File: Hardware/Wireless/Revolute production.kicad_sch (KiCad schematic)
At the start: 58 parts, among them J1 -, J2 +, Q1 NMOS-CSD17381F4, Q2 NMOS-CSD17381F4, Q3 PMOS-CSD25483F4, Q4 PMOS-CSD25483F4, Q5 PMOS-CSD25483F4, SW1 SW_Omron_B3FS, U10 BQ24075RGT, U11 MIC5504, U5 BQ27427, U6 nrf52833_qfn40, U8 Conn_01x14_Socket, U9 AS5600, X1 32.768 kHz, X2 32MHZ

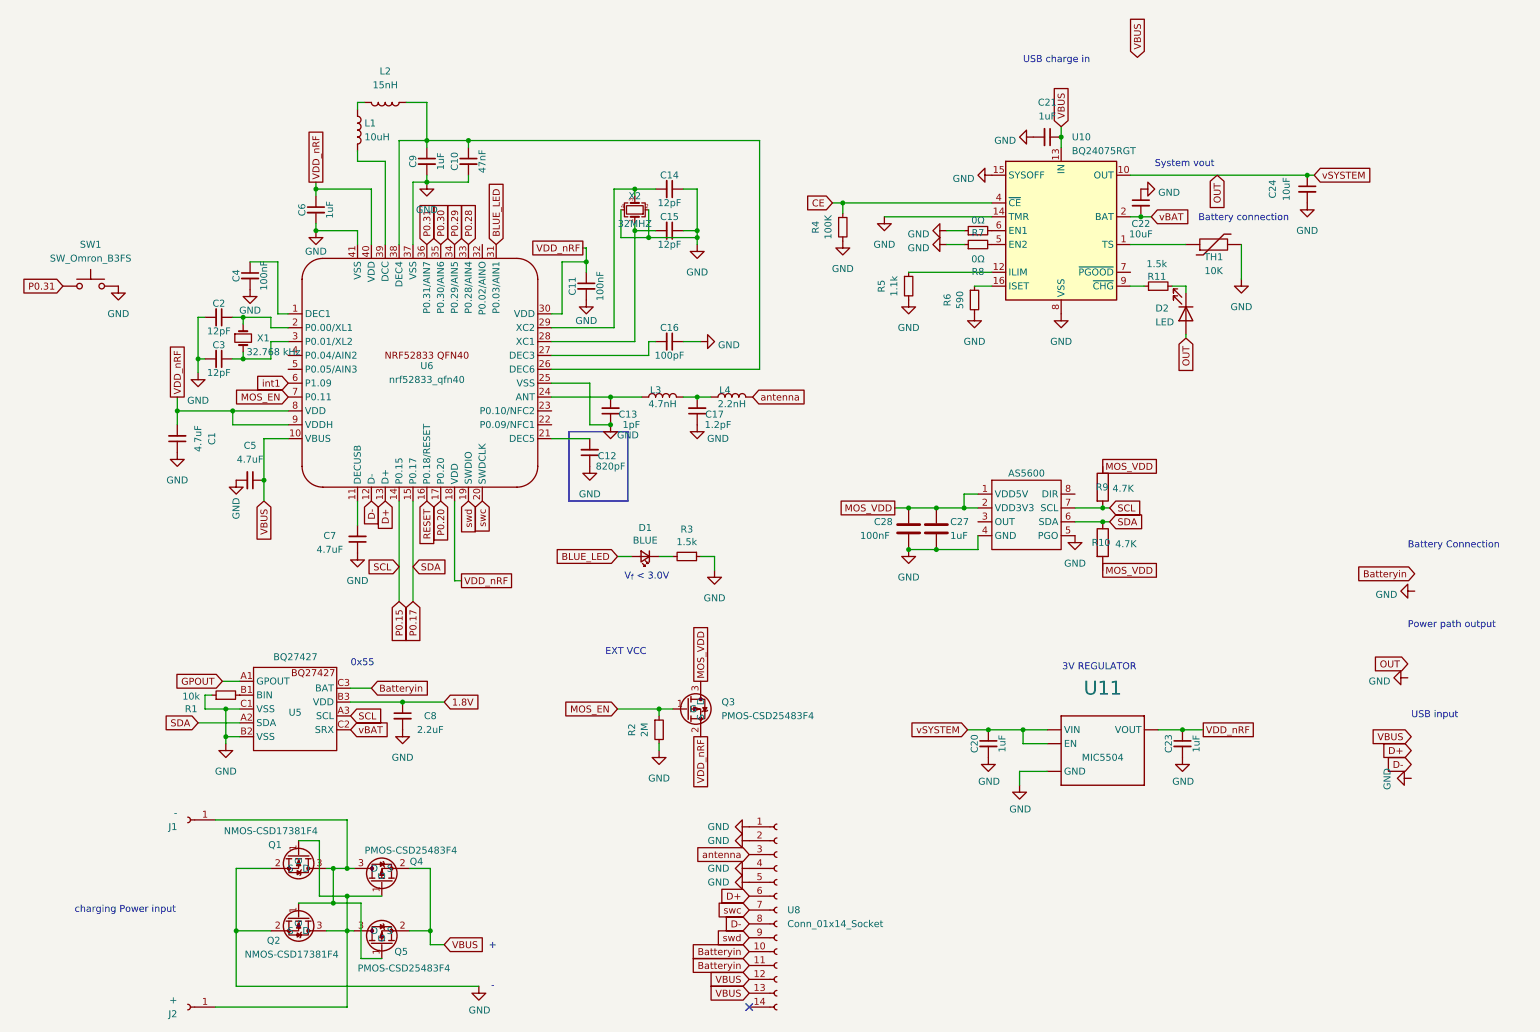
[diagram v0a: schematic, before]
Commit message: added status led
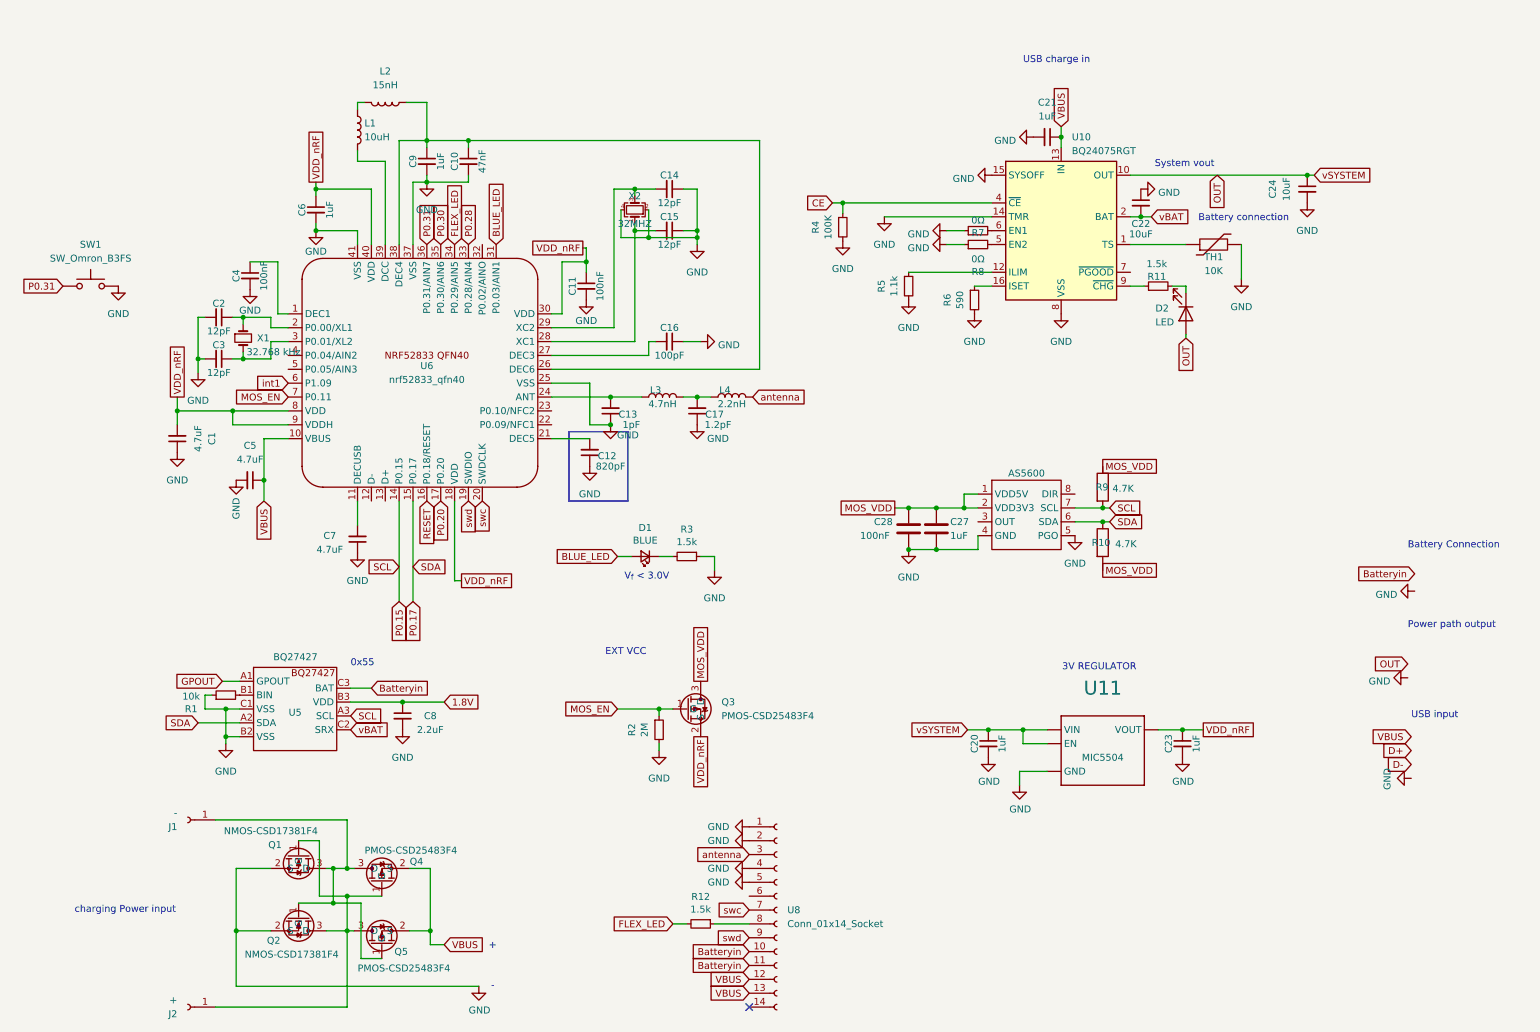
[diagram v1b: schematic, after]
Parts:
- added R12: 1.5k, Library:0402, symbol Device:R_Small
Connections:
- net D+: no longer U6.13 (D+), U8.6 (Pin_6)
- net D-: no longer U6.12 (D-), U8.8 (Pin_8)
- net P0.29 renamed FLEX_LED
- net FLEX_LED: now also R12.2
- new net: R12.1, U8.8 (Pin_8)
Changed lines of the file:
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@@
 	(wire
 		(pts
+			(xy 130.81 175.26) (xy 133.35 175.26)
+		)
+		(stroke
+			(width 0)
+			(type default)
+		)
+	)
+	(wire
+		(pts
 			(xy 214.63 58.42) (xy 217.17 58.42)
 		)
@@
 	(wire
 		(pts
+			(xy 138.43 175.26) (xy 144.78 175.26)
+		)
+		(stroke
+			(width 0)
+			(type default)
+		)
+	)
+	(wire
+		(pts
 			(xy 85.725 38.1) (xy 85.725 39.37)
 		)
@@
 		)
 	)
-	(global_label "D+"
-		(shape input)
-		(at 144.78 170.18 180)
-		(fields_autoplaced yes)
-		(effects
-			(font
-				(size 1.27 1.27)
-			)
-			(justify right)
-		)
-		(property "Intersheetrefs" "${INTERSHEET_REFS}"
-			(at 138.9524 170.18 0)
-			(effects
-				(font
-					(size 1.27 1.27)
-				)
-				(justify right)
-				(hide yes)
-			)
-		)
-	)
 	(global_label "RESET"
 		(shape input)
@@
 		)
 	)
-	(global_label "D-"
-		(shape input)
-		(at 75.565 97.79 270)
-		(fields_autoplaced yes)
-		(effects
-			(font
-				(size 1.27 1.27)
-			)
-			(justify right)
-		)
-		(property "Intersheetrefs" "${INTERSHEET_REFS}"
-			(at 75.565 103.5382 90)
-			(effects
-				(font
-					(size 1.27 1.27)
-				)
-				(justify right)
-				(hide yes)
-			)
-		)
-	)
 	(global_label "Batteryin"
 		(shape input)
@@
 		)
 	)
-	(global_label "D-"
-		(shape input)
-		(at 144.78 175.26 180)
-		(fields_autoplaced yes)
-		(effects
-			(font
-				(size 1.27 1.27)
-			)
-			(justify right)
-		)
-		(property "Intersheetrefs" "${INTERSHEET_REFS}"
-			(at 138.9524 175.26 0)
-			(effects
-				(font
-					(size 1.27 1.27)
-				)
-				(justify right)
-				(hide yes)
-			)
-		)
-	)
 	(global_label "vBAT"
 		(shape input)
@@
 		)
 	)
-	(global_label "D+"
-		(shape input)
-		(at 78.105 97.79 270)
-		(fields_autoplaced yes)
-		(effects
-			(font
-				(size 1.27 1.27)
-			)
-			(justify right)
-		)
-		(property "Intersheetrefs" "${INTERSHEET_REFS}"
-			(at 78.105 103.5382 90)
-			(effects
-				(font
-					(size 1.27 1.27)
-				)
-				(justify right)
-				(hide yes)
-			)
-		)
-	)
 	(global_label "MOS_VDD"
 		(shape passive)
@@
 		)
 	)
-	(global_label "VBUS"
-		(shape input)
-		(at 215.9 16.51 90)
-		(fields_autoplaced yes)
-		(effects
-			(font
-				(size 1.27 1.27)
-			)
-			(justify left)
-		)
-		(property "Intersheetrefs" "${INTERSHEET_REFS}"
-			(at 215.9 8.7056 90)
-			(effects
-				(font
-					(size 1.27 1.27)
-				)
-				(justify left)
-				(hide yes)
-			)
-		)
-	)
 	(global_label "CE"
 		(shape input)
@@
 		)
 	)
-	(global_label "P0.29"
-		(shape input)
-		(at 90.805 50.8 90)
-		(fields_autoplaced yes)
-		(effects
-			(font
-				(size 1.27 1.27)
-			)
-			(justify left)
-		)
-		(property "Intersheetrefs" "${INTERSHEET_REFS}"
-			(at 90.805 42.3909 90)
-			(effects
-				(font
-					(size 1.27 1.27)
-				)
-				(justify left)
-				(hide yes)
-			)
-		)
-	)
 	(global_label "VDD_nRF"
 		(shape passive)
@@
 		)
 	)
+	(global_label "FLEX_LED"
+		(shape input)
+		(at 130.81 175.26 180)
+		(fields_autoplaced yes)
+		(effects
+			(font
+				(size 1.27 1.27)
+			)
+			(justify right)
+		)
+		(property "Intersheetrefs" "${INTERSHEET_REFS}"
+			(at 118.9349 175.26 0)
+			(effects
+				(font
+					(size 1.27 1.27)
+				)
+				(justify right)
+				(hide yes)
+			)
+		)
+	)
+	(global_label "FLEX_LED"
+		(shape input)
+		(at 90.805 50.8 90)
+		(fields_autoplaced yes)
+		(effects
+			(font
+				(size 1.27 1.27)
+			)
+			(justify left)
+		)
+		(property "Intersheetrefs" "${INTERSHEET_REFS}"
+			(at 90.805 38.9249 90)
+			(effects
+				(font
+					(size 1.27 1.27)
+				)
+				(justify left)
+				(hide yes)
+			)
+		)
+	)
 	(global_label "VDD_nRF"
 		(shape passive)
@@
 					(unit 1)
 				)
+			)
+		)
+	)
+	(symbol
+		(lib_id "Device:R_Small")
+		(at 135.89 175.26 270)
+		(unit 1)
+		(exclude_from_sim no)
+		(in_bom yes)
+		(on_board yes)
+		(dnp no)
+		(property "Reference" "R12"
+			(at 135.89 170.2816 90)
+			(effects
+				(font
+					(size 1.27 1.27)
+				)
+			)
+		)
+		(property "Value" "1.5k"
+			(at 135.89 172.593 90)
+			(effects
+				(font
+					(size 1.27 1.27)
+				)
+			)
+		)
+		(property "Footprint" "Library:0402"
+			(at 135.89 175.26 0)
+			(effects
+				(font
+					(size 1.27 1.27)
+				)
+				(hide yes)
+			)
+		)
+		(property "Datasheet" "~"
+			(at 135.89 175.26 0)
+			(effects
+				(font
+					(size 1.27 1.27)
+				)
+				(hide yes)
+			)
+		)
+		(property "Description" "Resistor, small symbol"
+			(at 135.89 175.26 0)
+			(effects
+				(font
+					(size 1.27 1.27)
+				)
+				(hide yes)
+			)
+		)
+		(property "ID" "138"
+			(at 135.89 175.26 90)
+			(effects
+				(font
+					(size 1.27 1.27)
+				)
+				(hide yes)
+			)
+		)
+		(pin "1"
+		)
+		(pin "2"
+		)
+		(instances
+			(project "Revolute production"
+				(path "/4aa15f71-f105-4387-ae73-e687df291edc"
+					(reference "R12")
+					(unit 1)
+				)

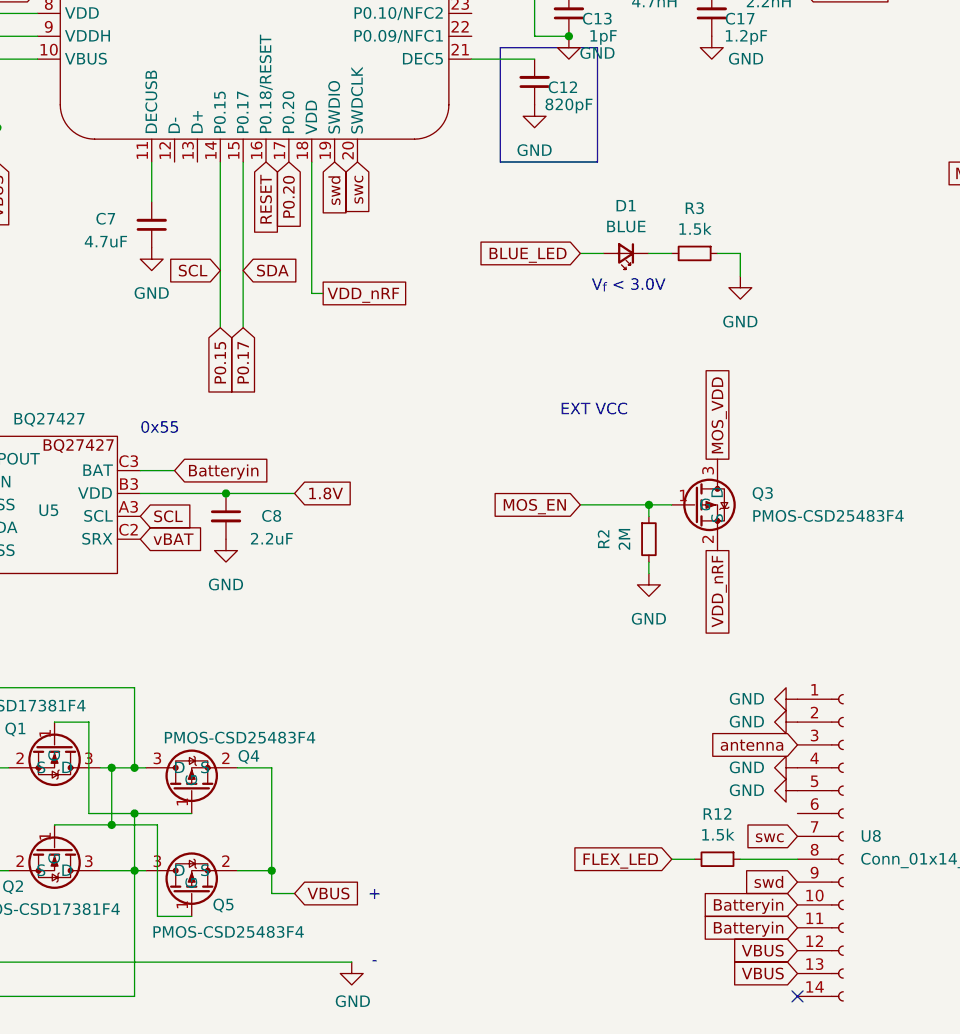
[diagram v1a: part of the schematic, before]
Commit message: revolute production boards
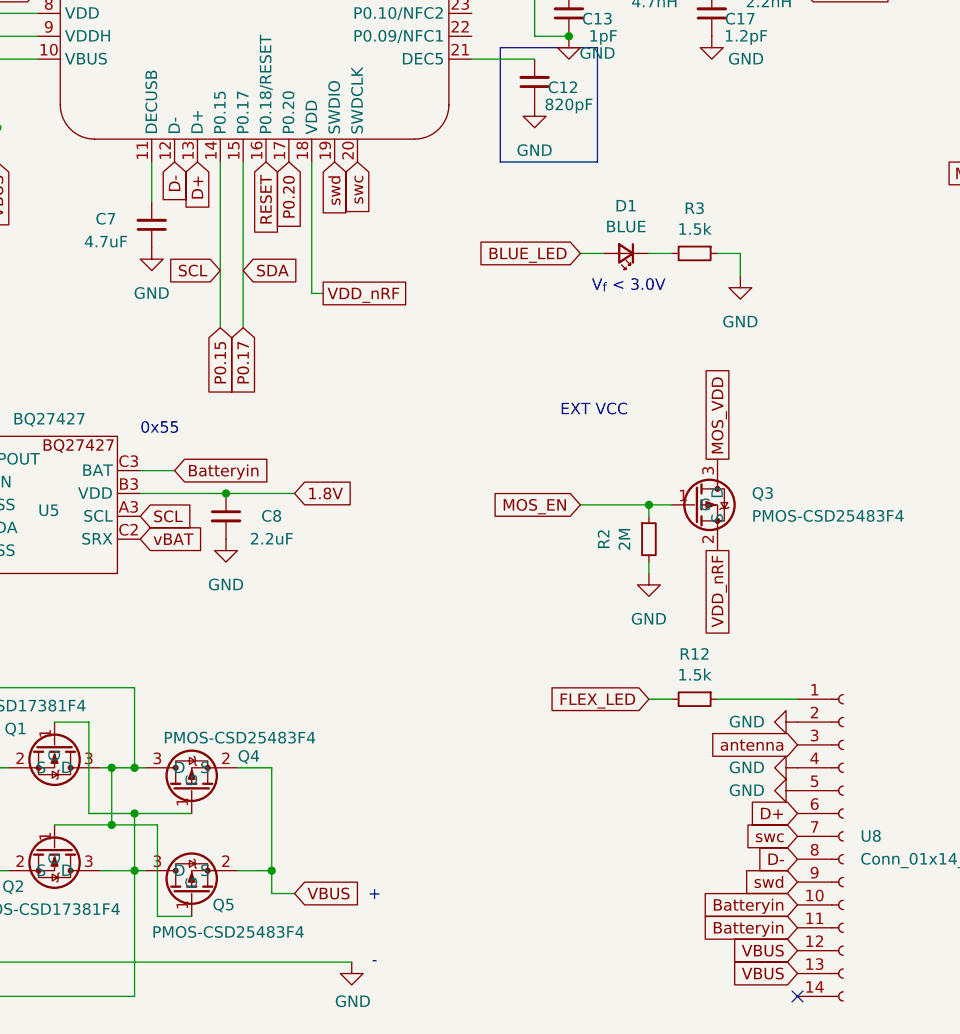
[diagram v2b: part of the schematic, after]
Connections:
- net D+: now also U6.13 (D+), U8.6 (Pin_6)
- net D-: now also U6.12 (D-), U8.8 (Pin_8)
- net GND: no longer U8.1 (Pin_1)
- net at R12.1: now also U8.1 (Pin_1); no longer U8.8 (Pin_8)
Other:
- moved on the sheet: R12
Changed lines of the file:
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@@
 	(wire
 		(pts
-			(xy 130.81 175.26) (xy 133.35 175.26)
+			(xy 128.27 157.48) (xy 130.81 157.48)
 		)
 		(stroke
@@
 	(wire
 		(pts
-			(xy 138.43 175.26) (xy 144.78 175.26)
+			(xy 135.89 157.48) (xy 144.78 157.48)
 		)
 		(stroke
@@
 		)
 	)
+	(global_label "D-"
+		(shape input)
+		(at 144.78 175.26 180)
+		(fields_autoplaced yes)
+		(effects
+			(font
+				(size 1.27 1.27)
+			)
+			(justify right)
+		)
+		(property "Intersheetrefs" "${INTERSHEET_REFS}"
+			(at 138.9524 175.26 0)
+			(effects
+				(font
+					(size 1.27 1.27)
+				)
+				(justify right)
+				(hide yes)
+			)
+		)
+	)
 	(global_label "OUT"
 		(shape input)
@@
 		)
 	)
+	(global_label "D+"
+		(shape input)
+		(at 78.105 97.79 270)
+		(fields_autoplaced yes)
+		(effects
+			(font
+				(size 1.27 1.27)
+			)
+			(justify right)
+		)
+		(property "Intersheetrefs" "${INTERSHEET_REFS}"
+			(at 78.105 103.5382 90)
+			(effects
+				(font
+					(size 1.27 1.27)
+				)
+				(justify right)
+				(hide yes)
+			)
+		)
+	)
+	(global_label "D-"
+		(shape input)
+		(at 75.565 97.79 270)
+		(fields_autoplaced yes)
+		(effects
+			(font
+				(size 1.27 1.27)
+			)
+			(justify right)
+		)
+		(property "Intersheetrefs" "${INTERSHEET_REFS}"
+			(at 75.565 103.5382 90)
+			(effects
+				(font
+					(size 1.27 1.27)
+				)
+				(justify right)
+				(hide yes)
+			)
+		)
+	)
 	(global_label "P0.31"
 		(shape input)
@@
 		)
 	)
+	(global_label "D+"
+		(shape input)
+		(at 144.78 170.18 180)
+		(fields_autoplaced yes)
+		(effects
+			(font
+				(size 1.27 1.27)
+			)
+			(justify right)
+		)
+		(property "Intersheetrefs" "${INTERSHEET_REFS}"
+			(at 138.9524 170.18 0)
+			(effects
+				(font
+					(size 1.27 1.27)
+				)
+				(justify right)
+				(hide yes)
+			)
+		)
+	)
 	(global_label "VBUS"
 		(shape input)
@@
 	(global_label "FLEX_LED"
 		(shape input)
-		(at 130.81 175.26 180)
+		(at 128.27 157.48 180)
 		(fields_autoplaced yes)
 		(effects
@@
 		)
 		(property "Intersheetrefs" "${INTERSHEET_REFS}"
-			(at 118.9349 175.26 0)
+			(at 116.3949 157.48 0)
 			(effects
 				(font
@@
 	(symbol
 		(lib_id "Device:R_Small")
-		(at 135.89 175.26 270)
+		(at 133.35 157.48 270)
 		(unit 1)
 		(exclude_from_sim no)
@@
 		(dnp no)
 		(property "Reference" "R12"
-			(at 135.89 170.2816 90)
+			(at 133.35 152.5016 90)
 			(effects
 				(font
@@
 		)
 		(property "Value" "1.5k"
-			(at 135.89 172.593 90)
+			(at 133.35 154.813 90)
 			(effects
 				(font
@@
 		)
 		(property "Footprint" "Library:0402"
-			(at 135.89 175.26 0)
+			(at 133.35 157.48 0)
 			(effects
 				(font
@@
 		)
 		(property "Datasheet" "~"
-			(at 135.89 175.26 0)
+			(at 133.35 157.48 0)
 			(effects
 				(font
@@
 		)
 		(property "Description" "Resistor, small symbol"
-			(at 135.89 175.26 0)
+			(at 133.35 157.48 0)
 			(effects
 				(font
@@
 		)
 		(property "ID" "138"
-			(at 135.89 175.26 90)
+			(at 133.35 157.48 90)
 			(effects
 				(font
@@
 	(symbol
 		(lib_id "power:GND")
+		(at 144.78 160.02 270)
+		(unit 1)
+		(exclude_from_sim no)
+		(in_bom yes)
+		(on_board yes)
+		(dnp no)
+		(property "Reference" "#PWR01"
+			(at 138.43 160.02 0)
+			(effects
+				(font
+					(size 1.27 1.27)
+				)
+				(hide yes)
+			)
+		)
+		(property "Value" "GND"
+			(at 137.16 160.02 90)
+			(effects
+				(font
+					(size 1.27 1.27)
+				)
+				(justify left)
+			)
+		)
+		(property "Footprint" ""
+			(at 144.78 160.02 0)
+			(effects
+				(font
+					(size 1.27 1.27)
+				)
+				(hide yes)
+			)
+		)
+		(property "Datasheet" ""
+			(at 144.78 160.02 0)
+			(effects
+				(font
+					(size 1.27 1.27)
+				)
+				(hide yes)
+			)
+		)
+		(property "Description" "Power symbol creates a global label with name \"GND\" , ground"
+			(at 144.78 160.02 0)
+			(effects
+				(font
+					(size 1.27 1.27)
+				)
+				(hide yes)
+			)
+		)
+		(pin "1"
+		)
+		(instances
+			(project "Revolute production"
+				(path "/4aa15f71-f105-4387-ae73-e687df291edc"
+					(reference "#PWR01")
+					(unit 1)
+				)
+			)
+		)
+	)
+	(symbol
+		(lib_id "power:GND")
 		(at 180.975 50.8 270)
 		(unit 1)
@@
 	(symbol
 		(lib_id "power:GND")
-		(at 144.78 157.48 270)
-		(unit 1)
-		(exclude_from_sim no)
-		(in_bom yes)
-		(on_board yes)
-		(dnp no)
-		(property "Reference" "#PWR023"
-			(at 138.43 157.48 0)
-			(effects
-				(font
-					(size 1.27 1.27)
-				)
-				(hide yes)
-			)
-		)
-		(property "Value" "GND"
-			(at 137.16 157.48 90)
-			(effects
-				(font
-					(size 1.27 1.27)
-				)
-				(justify left)
-			)
-		)
-		(property "Footprint" ""
-			(at 144.78 157.48 0)
-			(effects
-				(font
-					(size 1.27 1.27)
-				)
-				(hide yes)
-			)
-		)
-		(property "Datasheet" ""
-			(at 144.78 157.48 0)
-			(effects
-				(font
-					(size 1.27 1.27)
-				)
-				(hide yes)
-			)
-		)
-		(property "Description" "Power symbol creates a global label with name \"GND\" , ground"
-			(at 144.78 157.48 0)
-			(effects
-				(font
-					(size 1.27 1.27)
-				)
-				(hide yes)
-			)
-		)
-		(pin "1"
-		)
-		(instances
-			(project "Revolute production"
-				(path "/4aa15f71-f105-4387-ae73-e687df291edc"
-					(reference "#PWR023")
-					(unit 1)
-				)
-			)
-		)
-	)
-	(symbol
-		(lib_id "power:GND")
 		(at 173.99 60.96 0)
 		(unit 1)
@@
 					(unit 1)
 				)
-			)
-		)
-	)
-	(symbol
-		(lib_id "power:GND")
-		(at 144.78 160.02 270)
-		(unit 1)
-		(exclude_from_sim no)
-		(in_bom yes)
-		(on_board yes)
-		(dnp no)
-		(property "Reference" "#PWR024"
-			(at 138.43 160.02 0)
-			(effects
-				(font
-					(size 1.27 1.27)
-				)
-				(hide yes)
-			)
-		)
-		(property "Value" "GND"
-			(at 137.16 160.02 90)
-			(effects
-				(font
-					(size 1.27 1.27)
-				)
-				(justify left)
-			)
-		)
-		(property "Footprint" ""
-			(at 144.78 160.02 0)
-			(effects
-				(font
-					(size 1.27 1.27)
-				)
-				(hide yes)
-			)
-		)
-		(property "Datasheet" ""
-			(at 144.78 160.02 0)
-			(effects
-				(font
-					(size 1.27 1.27)
-				)
-				(hide yes)
-			)
-		)
-		(property "Description" "Power symbol creates a global label with name \"GND\" , ground"
-			(at 144.78 160.02 0)
-			(effects
-				(font
-					(size 1.27 1.27)
-				)
-				(hide yes)
-			)
-		)
-		(pin "1"
-		)
-		(instances
-			(project "Revolute production"
-				(path "/4aa15f71-f105-4387-ae73-e687df291edc"
-					(reference "#PWR024")
-					(unit 1)
-				)
